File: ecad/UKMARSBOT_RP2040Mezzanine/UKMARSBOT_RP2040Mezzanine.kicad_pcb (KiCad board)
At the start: 2 copper layers, 63 x 80 mm, 16 parts, among them J1 Conn_01x16, J2 Conn_01x06, J3 Conn_01x06, J4 Conn_01x06, J5 Conn_01x04_Pin, SW1 TACT_SW, SW2 TACT_SW, U1 Pico

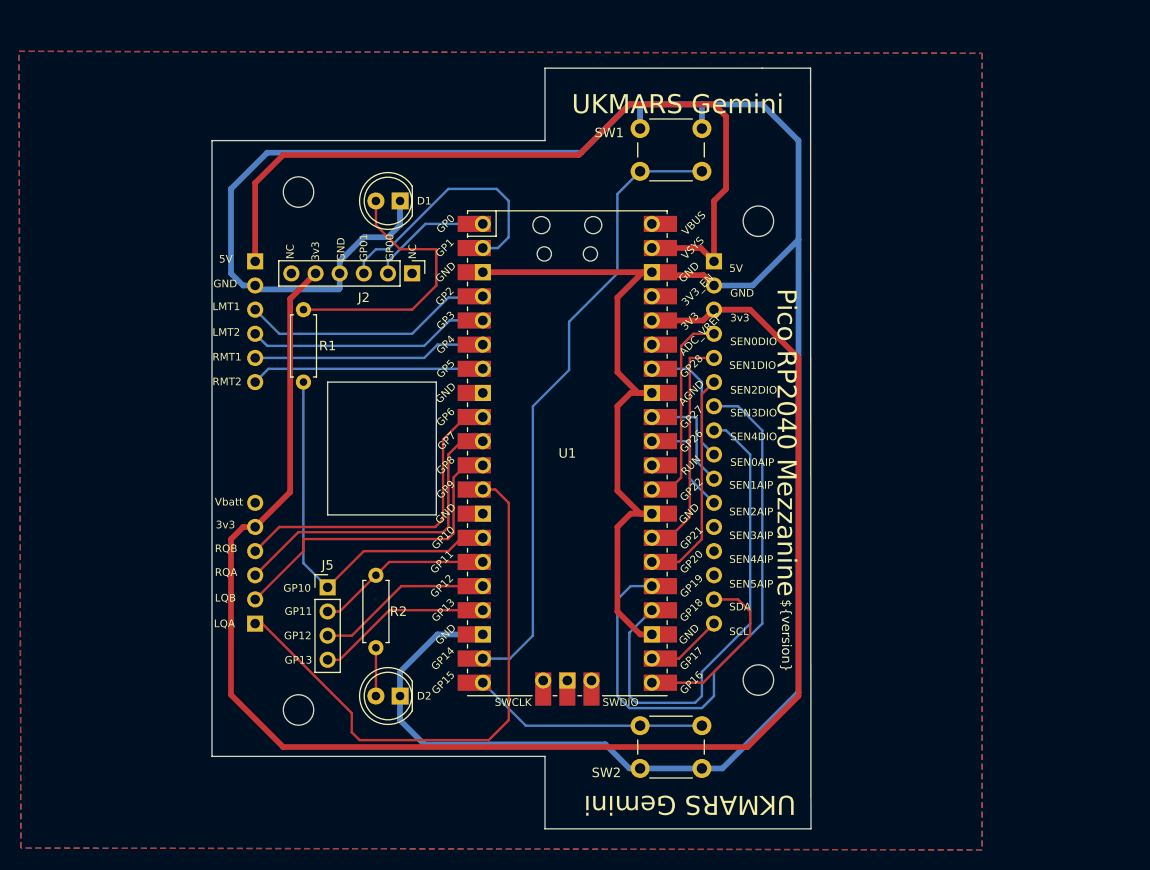
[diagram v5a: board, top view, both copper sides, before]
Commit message: Updated Chassis and Mezzanine board - Sensor boards need to reflect new connector position
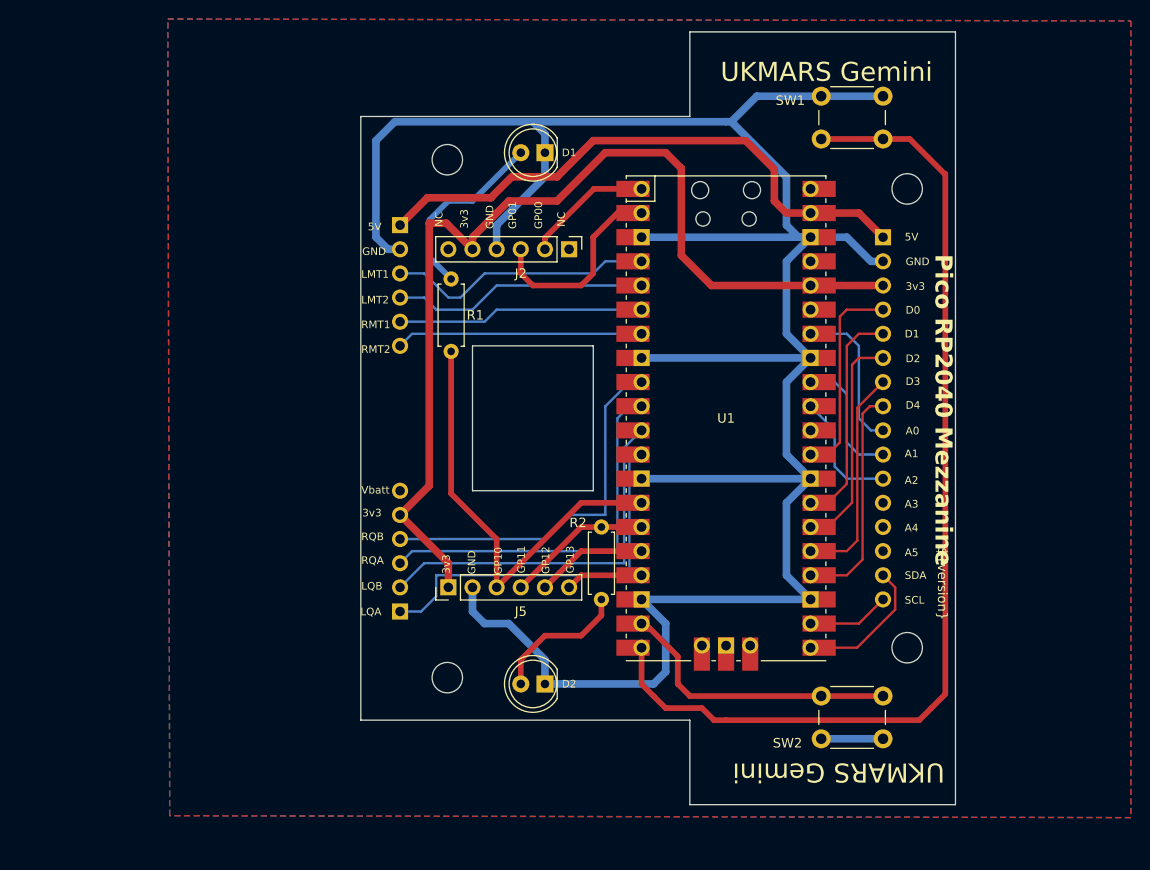
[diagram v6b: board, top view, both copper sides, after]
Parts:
- J5: value Conn_01x04_Pin -> Conn_01x06; footprint Connector_PinHeader_2.54mm:PinHeader_1x04_P2.54mm_Vertical -> Connector_PinHeader_2.54mm:PinHeader_1x06_P2.54mm_Vertical
- R1, R2: value 330R -> 680R
- moved R2 24.3 mm to (127.9, 113.0)
- moved SW1 19.4 mm to (151.0, 67.7)
- moved SW2 19.3 mm to (157.5, 135.3)
- moved J1 18.0 mm to (157.5, 82.5)
- moved U1 17.1 mm to (141.0, 101.6)
- moved J2 16.7 mm to (124.5, 83.8)
- moved D1 16.1 mm to (121.9, 73.7)
- moved H2 16.0 mm to (111.7, 128.9)
- moved H3 16.0 mm to (160.0, 77.5)
- moved H1 16.0 mm to (111.7, 74.4)
- moved H4 16.0 mm to (160.0, 125.7)
- moved R1 15.9 mm to (112.1, 94.6)
- moved J3 15.7 mm to (106.7, 81.3)
- moved J4 15.3 mm to (106.7, 121.9)
- moved D2 15.3 mm to (121.9, 129.5)
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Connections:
- J5 pad 1: GPIO10 -> 3v3
- J5 pad 2: GPIO11 -> GND
- J5 pad 3: GPIO12 -> GPIO10
- J5 pad 4: GPIO13 -> GPIO11
- SW1 pad 2: GPIO14 -> GPIO15
- SW2 pad 2: GPIO15 -> GPIO14
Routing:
- net GPIO15: track 24.9 -> 107.8 mm
- net 3v3: track 166.5 -> 106.6 mm
- net GND: track 313.6 -> 268.3 mm
- net SEN3DI0: track 61.8 -> 23.2 mm
- net GPIO14: track 66.3 -> 30.3 mm
- net SEN4DI0: track 50.6 -> 24.0 mm
- net 5V: track 84.6 -> 60.6 mm
- net LQA: track 60.0 -> 41.0 mm
- net GPIO13: track 18.5 -> 8.15 mm
- net Net-(D2-A): track 5.08 -> 14.6 mm
- net Net-(D1-A): track 28.8 -> 19.7 mm
- net GPIO12: track 18.5 -> 11.7 mm
- net RQA: track 34.2 -> 40.4 mm
- net GPIO01: track 27.2 -> 21.2 mm
- net GPIO10: track 41.1 -> 45.7 mm
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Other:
- board size 63 x 80 mm -> 62.5 x 81.3 mm
- board text added: "A0"
- board text added: "A1"
- board text added: "A2"
- board text added: "A3"
- board text added: "A4"
- board text added: "A5"
- board text added: "D0"
- board text added: "D1"
- board text added: "D2"
- board text added: "D3"
- board text added: "D4"
- board text removed: "SEN0AIP"
- board text removed: "SEN0DIO"
- board text removed: "SEN1AIP"
- board text removed: "SEN1DIO"
- board text removed: "SEN2AIP"
- board text removed: "SEN2DIO"
- board text removed: "SEN3AIP"
- board text removed: "SEN3DIO"
- board text removed: "SEN4AIP"
- board text removed: "SEN4DIO"
- board text removed: "SEN5AIP"
